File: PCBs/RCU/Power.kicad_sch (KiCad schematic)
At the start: 35 parts, among them J100 Conn_01x02, U100 AP63203WU, U102 AZ1117-3.3, U103 AP63203WU, U104 LM2576S-ADJ

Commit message: Schematic cleanup
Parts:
- C102, C112: value 10u -> (none)
- C106, C107, C110, C111: value 1u -> (none)
- C116: value 100u -> (none)
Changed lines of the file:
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@@
       (effects (font (size 1.27 1.27)) (justify left))
     )
-    (property "Value" "1u" (id 1) (at 92.71 149.86 0)
+    (property "Value" "" (id 1) (at 92.71 149.86 0)
       (effects (font (size 1.27 1.27)) (justify left))
     )
@@
       (effects (font (size 1.27 1.27)) (justify left))
     )
-    (property "Value" "1u" (id 1) (at 90.17 104.14 0)
+    (property "Value" "" (id 1) (at 90.17 104.14 0)
       (effects (font (size 1.27 1.27)) (justify left))
     )
@@
       (effects (font (size 1.27 1.27)) (justify left))
     )
-    (property "Value" "10u" (id 1) (at 198.12 62.23 0)
+    (property "Value" "" (id 1) (at 198.12 62.23 0)
       (effects (font (size 1.27 1.27)) (justify left))
     )
@@
       (effects (font (size 1.27 1.27)) (justify left))
     )
-    (property "Value" "10u" (id 1) (at 196.85 147.32 0)
+    (property "Value" "" (id 1) (at 196.85 147.32 0)
       (effects (font (size 1.27 1.27)) (justify left))
     )
@@
       (effects (font (size 1.27 1.27)) (justify left))
     )
-    (property "Value" "1u" (id 1) (at 119.38 104.14 0)
+    (property "Value" "" (id 1) (at 119.38 104.14 0)
       (effects (font (size 1.27 1.27)) (justify left))
     )
@@
       (effects (font (size 1.27 1.27)) (justify left))
     )
-    (property "Value" "100u" (id 1) (at 189.23 198.12 0)
+    (property "Value" "" (id 1) (at 189.23 198.12 0)
       (effects (font (size 1.27 1.27)) (justify left))
     )
@@
       (effects (font (size 1.27 1.27)) (justify left))
     )
-    (property "Value" "1u" (id 1) (at 121.92 149.86 0)
-      (effects (font (size 1.27 1.27)) (justify left))
-    )
+    (property "Value" "" (id 1) (at 121.92 149.86 0)
+      (effects (font (size 1.27 1.27)) (justify left))
+    )

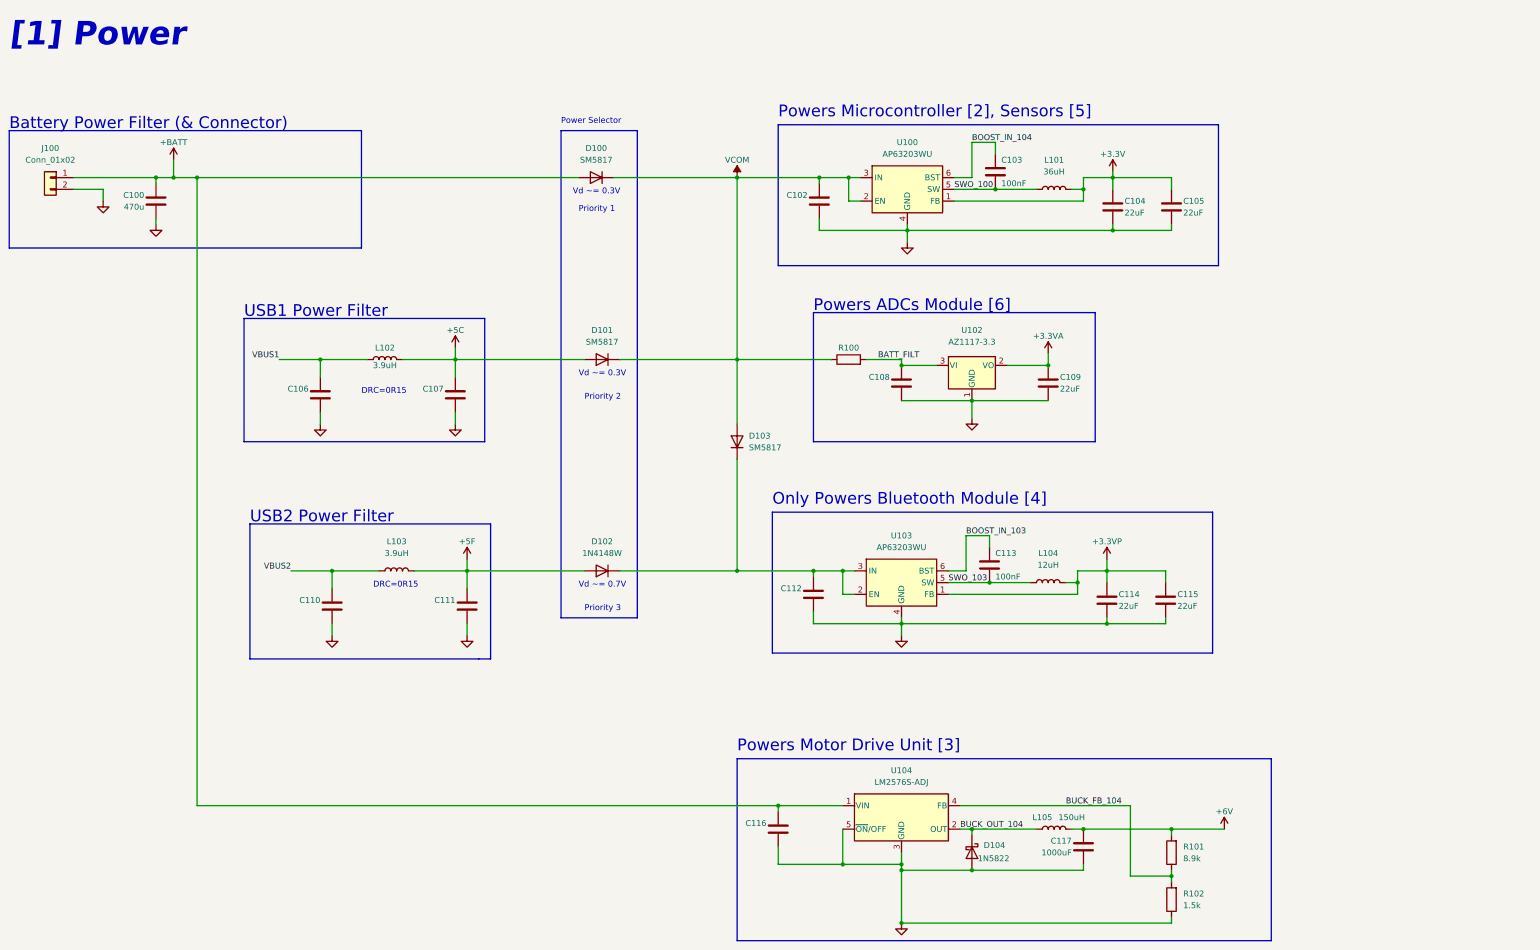
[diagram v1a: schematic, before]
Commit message: Wrote that first regulator in power schematic also powers the external memory
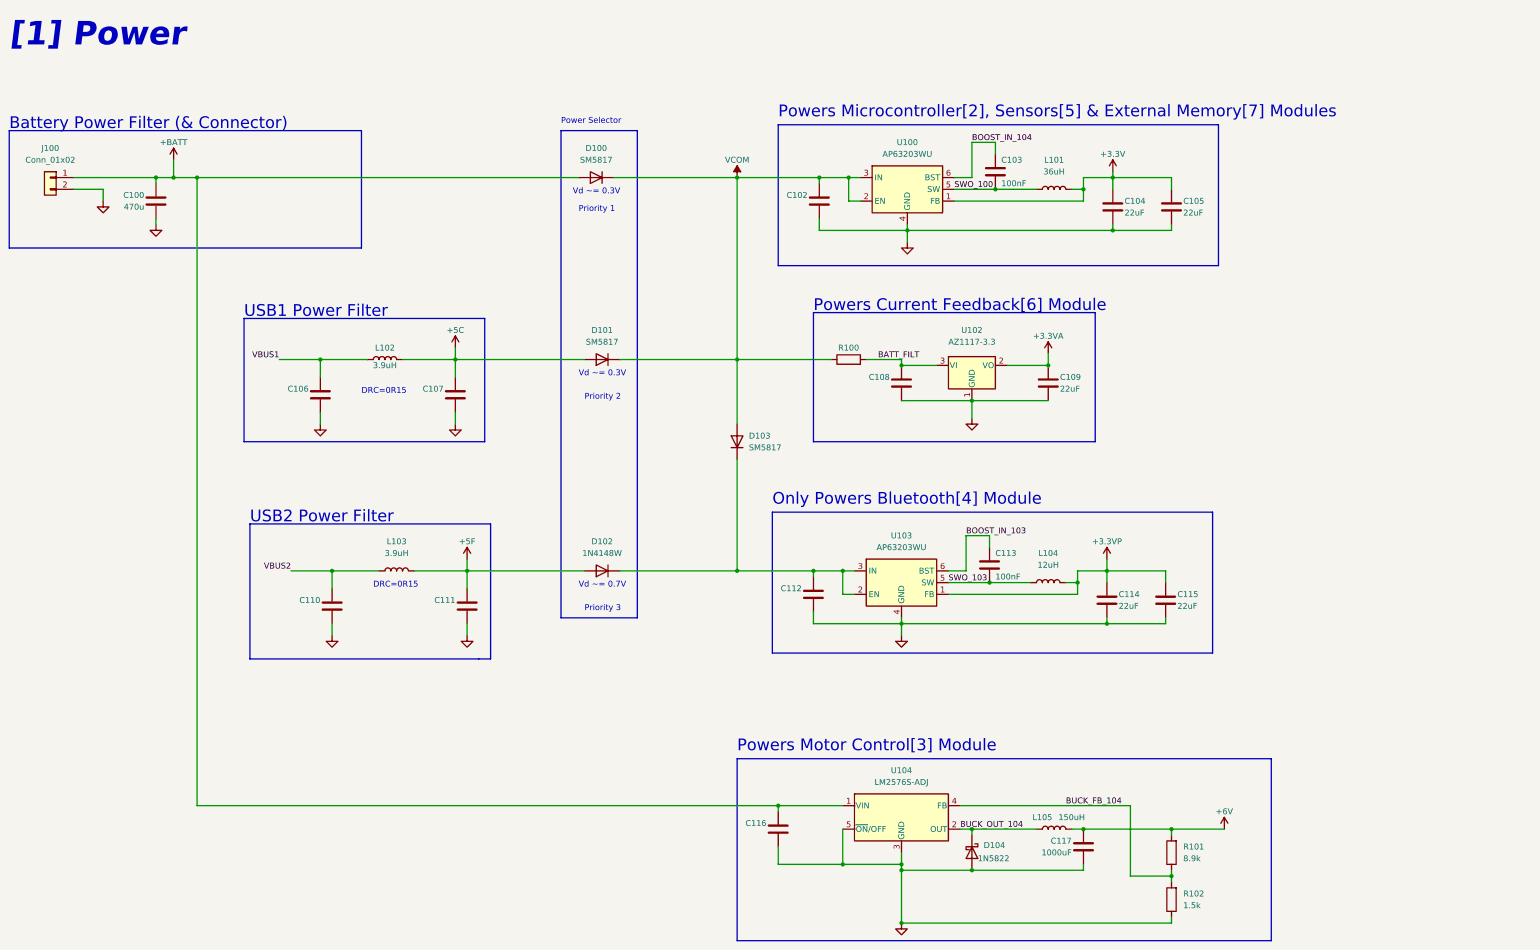
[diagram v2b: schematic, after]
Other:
- note added: "Only Powers Bluetooth[4] Module"
- note added: "Powers Current Feedback[6] Module"
- note added: "Powers Microcontroller[2], Sensors[5] & External Memory[7] Modules"
- note added: "Powers Motor Control[3] Module"
- note removed: "Only Powers Bluetooth Module [4]"
- note removed: "Powers ADCs Module [6]"
- note removed: "Powers Microcontroller [2], Sensors [5]"
- note removed: "Powers Motor Drive Unit [3]"
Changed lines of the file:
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@@
     (effects (font (size 1.27 1.27)) (justify left bottom))
   )
-  (text "Powers Microcontroller [2], Sensors [5]" (at 191.77 43.18 0)
+  (text "Powers Microcontroller[2], Sensors[5] & External Memory[7] Modules"
+    (at 191.77 43.18 0)
     (effects (font (size 2.54 2.54)) (justify left bottom))
   )
@@
     (effects (font (size 1.27 1.27)) (justify left bottom))
   )
-  (text "Powers ADCs Module [6]" (at 199.39 85.09 0)
+  (text "Powers Current Feedback[6] Module " (at 199.39 85.09 0)
     (effects (font (size 2.54 2.54)) (justify left bottom))
   )
-  (text "Only Powers Bluetooth Module [4]" (at 190.5 127 0)
+  (text "Only Powers Bluetooth[4] Module " (at 190.5 127 0)
     (effects (font (size 2.54 2.54)) (justify left bottom))
   )
@@
     (effects (font (size 5.08 5.08) (thickness 1.016) bold italic) (justify left bottom))
   )
-  (text "Powers Motor Drive Unit [3]" (at 182.88 180.34 0)
+  (text "Powers Motor Control[3] Module" (at 182.88 180.34 0)
     (effects (font (size 2.54 2.54)) (justify left bottom))
   )

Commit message: Corrected SPI_MOSI and SPI_MISO labels on U700 - external memory
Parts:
- C102, C112: value (none) -> 10uF
- C106, C107, C110, C111: value (none) -> 1uF
- C108: value (none) -> 22uF
- C116: value (none) -> 100uF
- R100: value (none) -> 5R
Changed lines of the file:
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@@
       (effects (font (size 1.27 1.27)) (justify left))
     )
-    (property "Value" "" (id 1) (at 92.71 149.86 0)
+    (property "Value" "1uF" (id 1) (at 92.71 149.86 0)
       (effects (font (size 1.27 1.27)) (justify left))
     )
@@
       (effects (font (size 1.27 1.27)) (justify left))
     )
-    (property "Value" "" (id 1) (at 215.9 101.6 0)
+    (property "Value" "22uF" (id 1) (at 215.9 101.6 0)
       (effects (font (size 1.27 1.27)) (justify left))
     )
@@
       (effects (font (size 1.27 1.27)) (justify left))
     )
-    (property "Value" "" (id 1) (at 90.17 104.14 0)
+    (property "Value" "1uF" (id 1) (at 90.17 104.14 0)
       (effects (font (size 1.27 1.27)) (justify left))
     )
@@
       (effects (font (size 1.27 1.27)) (justify left))
     )
-    (property "Value" "" (id 1) (at 198.12 62.23 0)
+    (property "Value" "10uF" (id 1) (at 198.12 62.23 0)
       (effects (font (size 1.27 1.27)) (justify left))
     )
@@
       (effects (font (size 1.27 1.27)) (justify left))
     )
-    (property "Value" "" (id 1) (at 196.85 147.32 0)
+    (property "Value" "10uF" (id 1) (at 196.85 147.32 0)
       (effects (font (size 1.27 1.27)) (justify left))
     )
@@
       (effects (font (size 1.27 1.27)) (justify left))
     )
-    (property "Value" "" (id 1) (at 119.38 104.14 0)
+    (property "Value" "1uF" (id 1) (at 119.38 104.14 0)
       (effects (font (size 1.27 1.27)) (justify left))
     )
@@
       (effects (font (size 1.27 1.27)) (justify left))
     )
-    (property "Value" "" (id 1) (at 189.23 198.12 0)
+    (property "Value" "100uF" (id 1) (at 189.23 198.12 0)
       (effects (font (size 1.27 1.27)) (justify left))
     )
@@
     (in_bom yes) (on_board yes)
     (property "Reference" "R100" (id 0) (at 207.01 92.71 90))
-    (property "Value" "" (id 1) (at 207.01 97.79 90))
+    (property "Value" "5R" (id 1) (at 207.01 97.79 90))
     (property "Footprint" "" (id 2) (at 207.01 97.028 90)
       (effects (font (size 1.27 1.27)) hide)
@@
       (effects (font (size 1.27 1.27)) (justify left))
     )
-    (property "Value" "" (id 1) (at 121.92 149.86 0)
-      (effects (font (size 1.27 1.27)) (justify left))
-    )
+    (property "Value" "1uF" (id 1) (at 121.92 149.86 0)
+      (effects (font (size 1.27 1.27)) (justify left))
+    )

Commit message: Have footprints for all power ICs
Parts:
- U102: value AZ1117-3.3 -> (none)
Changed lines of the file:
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@@
     (in_bom yes) (on_board yes) (fields_autoplaced)
     (property "Reference" "U102" (id 0) (at 233.68 88.9 0))
-    (property "Value" "AZ1117-3.3" (id 1) (at 233.68 91.44 0))
+    (property "Value" "" (id 1) (at 233.68 91.44 0))
     (property "Footprint" "" (id 2) (at 233.68 90.17 0)
       (effects (font (size 1.27 1.27) italic) hide)

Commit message: Add footprint to power module diodes, and replaced 1N4148W with 2 SM5817's
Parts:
- removed D102: 1N4148W, Diode_SMD:D_SOD-123, symbol Diode:1N4148W
- added D103, D104: SM5817, Schottky_Diode:SODFL3719X135N, symbol Diode:SM513
- D100, D101: value SM5817 -> (none)
- D102: renamed from D103; value SM5817 -> (none)
- U102: value (none) -> AZ1117-3.3; footprint (none) -> Package_TO_SOT_SMD:TO-252-2
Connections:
- net +5F: now also D103.2 (A)
- net at C112.1, D102.1 (K), U103.2 (EN)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: now also D104.1 (K)
- new net: D103.1 (K), D104.2 (A)
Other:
- note added: "Vd ~= 0.6V"
- note removed: "Vd ~= 0.7V"
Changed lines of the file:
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@@
   (junction (at 276.86 196.85) (diameter 0) (color 0 0 0 0)
   )
+  (junction (at 218.44 204.47) (diameter 0) (color 0 0 0 0)
+  )
+  (junction (at 264.16 55.88) (diameter 0) (color 0 0 0 0)
+  )
+  (junction (at 262.89 152.4) (diameter 0) (color 0 0 0 0)
+  )
+  (junction (at 238.76 58.42) (diameter 0) (color 0 0 0 0)
+  )
+  (junction (at 218.44 96.52) (diameter 0) (color 0 0 0 0)
+  )
+  (junction (at 60.96 55.88) (diameter 0) (color 0 0 0 0)
+  )
+  (junction (at 205.74 204.47) (diameter 0) (color 0 0 0 0)
+  )
+  (junction (at 233.68 104.14) (diameter 0) (color 0 0 0 0)
+  )
   (junction (at 182.88 140.97) (diameter 0) (color 0 0 0 0)
   )
-  (junction (at 218.44 204.47) (diameter 0) (color 0 0 0 0)
-  )
-  (junction (at 264.16 55.88) (diameter 0) (color 0 0 0 0)
-  )
-  (junction (at 262.89 152.4) (diameter 0) (color 0 0 0 0)
-  )
-  (junction (at 238.76 58.42) (diameter 0) (color 0 0 0 0)
-  )
-  (junction (at 218.44 96.52) (diameter 0) (color 0 0 0 0)
-  )
-  (junction (at 60.96 55.88) (diameter 0) (color 0 0 0 0)
-  )
-  (junction (at 205.74 204.47) (diameter 0) (color 0 0 0 0)
-  )
-  (junction (at 233.68 104.14) (diameter 0) (color 0 0 0 0)
-  )
   (junction (at 95.25 140.97) (diameter 0) (color 0 0 0 0)
   )
@@
     (stroke (width 0) (type default) (color 0 0 0 0))
   )
-  (polyline (pts (xy 144.78 45.72) (xy 161.29 45.72))
+  (polyline (pts (xy 143.51 45.72) (xy 162.56 45.72))
     (stroke (width 0) (type default) (color 0 0 0 0))
   )
@@
     (stroke (width 0) (type default) (color 0 0 0 0))
   )
+  (wire (pts (xy 153.67 140.97) (xy 152.4 140.97))
+    (stroke (width 0) (type default) (color 0 0 0 0))
+  )
   (wire (pts (xy 182.88 95.25) (xy 203.2 95.25))
     (stroke (width 0) (type default) (color 0 0 0 0))
@@
     (stroke (width 0) (type default) (color 0 0 0 0))
   )
-  (polyline (pts (xy 144.78 151.13) (xy 161.29 151.13))
+  (polyline (pts (xy 143.51 151.13) (xy 162.56 151.13))
     (stroke (width 0) (type default) (color 0 0 0 0))
   )
@@
     (stroke (width 0) (type default) (color 0 0 0 0))
   )
-  (polyline (pts (xy 144.78 45.72) (xy 144.78 151.13))
+  (polyline (pts (xy 143.51 45.72) (xy 143.51 151.13))
     (stroke (width 0) (type default) (color 0 0 0 0))
   )
@@
     (stroke (width 0) (type default) (color 0 0 0 0))
   )
-  (polyline (pts (xy 161.29 151.13) (xy 161.29 45.72))
+  (polyline (pts (xy 162.56 151.13) (xy 162.56 45.72))
     (stroke (width 0) (type default) (color 0 0 0 0))
   )
@@
     (stroke (width 0) (type default) (color 0 0 0 0))
   )
+  (wire (pts (xy 124.46 140.97) (xy 144.78 140.97))
+    (stroke (width 0) (type default) (color 0 0 0 0))
+  )
+  (wire (pts (xy 161.29 140.97) (xy 182.88 140.97))
+    (stroke (width 0) (type default) (color 0 0 0 0))
+  )
   (wire (pts (xy 110.49 95.25) (xy 121.92 95.25))
     (stroke (width 0) (type default) (color 0 0 0 0))
@@
     (stroke (width 0) (type default) (color 0 0 0 0))
   )
-  (wire (pts (xy 124.46 140.97) (xy 149.86 140.97))
-    (stroke (width 0) (type default) (color 0 0 0 0))
-  )
   (polyline (pts (xy 128.27 113.03) (xy 76.2 113.03))
     (stroke (width 0) (type default) (color 0 0 0 0))
@@
   )
   (polyline (pts (xy 191.77 74.93) (xy 287.02 74.93))
-    (stroke (width 0) (type default) (color 0 0 0 0))
-  )
-  (wire (pts (xy 157.48 140.97) (xy 182.88 140.97))
     (stroke (width 0) (type default) (color 0 0 0 0))
   )
@@
     (effects (font (size 1.27 1.27)) (justify left bottom))
   )
-  (text "Vd ~= 0.7V" (at 148.59 144.78 0)
+  (text "Vd ~= 0.6V" (at 148.59 144.78 0)
     (effects (font (size 1.27 1.27)) (justify left bottom))
   )
@@
     (pin "2")
   )
+  (symbol (lib_id "Diode:SM513") (at 157.48 140.97 180) (unit 1)
+    (in_bom yes) (on_board yes) (fields_autoplaced)
+    (property "Reference" "D104" (id 0) (at 157.48 134.62 0))
+    (property "Value" "SM5817" (id 1) (at 157.48 137.16 0))
+    (property "Footprint" "Schottky_Diode:SODFL3719X135N" (id 2) (at 157.48 136.525 0)
+      (effects (font (size 1.27 1.27)) hide)
+    )
+    (property "Datasheet" "http://cdn-reichelt.de/documents/datenblatt/A400/SMD1N400%23DIO.pdf" (id 3) (at 157.48 140.97 0)
+      (effects (font (size 1.27 1.27)) hide)
+    )
+    (pin "1")
+    (pin "2")
+  )
   (symbol (lib_id "power:GND") (at 57.15 66.04 0) (unit 1)
     (in_bom yes) (on_board yes) (fields_autoplaced)
@@
     )
     (pin "1")
-  )
-  (symbol (lib_id "Diode:1N4148W") (at 153.67 140.97 180) (unit 1)
-    (in_bom yes) (on_board yes) (fields_autoplaced)
-    (property "Reference" "D102" (id 0) (at 153.67 134.62 0))
-    (property "Value" "1N4148W" (id 1) (at 153.67 137.16 0))
-    (property "Footprint" "Diode_SMD:D_SOD-123" (id 2) (at 153.67 136.525 0)
-      (effects (font (size 1.27 1.27)) hide)
-    )
-    (property "Datasheet" "https://www.vishay.com/docs/85748/1n4148w.pdf" (id 3) (at 153.67 140.97 0)
-      (effects (font (size 1.27 1.27)) hide)
-    )
-    (pin "1")
-    (pin "2")
   )
   (symbol (lib_id "power:+3.3VA") (at 250.19 93.98 0) (unit 1)
@@
     (pin "1")
   )
+  (symbol (lib_id "Diode:SM513") (at 148.59 140.97 180) (unit 1)
+    (in_bom yes) (on_board yes) (fields_autoplaced)
+    (property "Reference" "D103" (id 0) (at 148.59 134.62 0))
+    (property "Value" "SM5817" (id 1) (at 148.59 137.16 0))
+    (property "Footprint" "Schottky_Diode:SODFL3719X135N" (id 2) (at 148.59 136.525 0)
+      (effects (font (size 1.27 1.27)) hide)
+    )
+    (property "Datasheet" "http://cdn-reichelt.de/documents/datenblatt/A400/SMD1N400%23DIO.pdf" (id 3) (at 148.59 140.97 0)
+      (effects (font (size 1.27 1.27)) hide)
+    )
+    (pin "1")
+    (pin "2")
+  )
   (symbol (lib_id "power:GND") (at 218.44 217.17 0) (unit 1)
     (in_bom yes) (on_board yes) (fields_autoplaced)
@@
     (in_bom yes) (on_board yes) (fields_autoplaced)
     (property "Reference" "U102" (id 0) (at 233.68 88.9 0))
-    (property "Value" "" (id 1) (at 233.68 91.44 0))
-    (property "Footprint" "" (id 2) (at 233.68 90.17 0)
+    (property "Value" "AZ1117-3.3" (id 1) (at 233.68 91.44 0))
+    (property "Footprint" "Package_TO_SOT_SMD:TO-252-2" (id 2) (at 233.68 90.17 0)
       (effects (font (size 1.27 1.27) italic) hide)
     )
@@
     (in_bom yes) (on_board yes) (fields_autoplaced)
     (property "Reference" "D100" (id 0) (at 152.4 49.53 0))
-    (property "Value" "SM5817" (id 1) (at 152.4 52.07 0))
+    (property "Value" "" (id 1) (at 152.4 52.07 0))
     (property "Footprint" "" (id 2) (at 152.4 51.435 0)
       (effects (font (size 1.27 1.27)) hide)
@@
   (symbol (lib_id "Diode:SM513") (at 182.88 113.03 90) (unit 1)
     (in_bom yes) (on_board yes) (fields_autoplaced)
-    (property "Reference" "D103" (id 0) (at 185.42 111.7599 90)
+    (property "Reference" "D102" (id 0) (at 185.42 111.7599 90)
       (effects (font (size 1.27 1.27)) (justify right))
     )
-    (property "Value" "SM5817" (id 1) (at 185.42 114.2999 90)
+    (property "Value" "" (id 1) (at 185.42 114.2999 90)
       (effects (font (size 1.27 1.27)) (justify right))
     )
@@
     (in_bom yes) (on_board yes) (fields_autoplaced)
     (property "Reference" "D101" (id 0) (at 153.67 88.9 0))
-    (property "Value" "SM5817" (id 1) (at 153.67 91.44 0))
+    (property "Value" "" (id 1) (at 153.67 91.44 0))
     (property "Footprint" "" (id 2) (at 153.67 90.805 0)
       (effects (font (size 1.27 1.27)) hide)

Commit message: Add soler wire connections for battery power
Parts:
- J100: value Conn_01x02 -> (none)
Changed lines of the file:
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@@
     (in_bom yes) (on_board yes) (fields_autoplaced)
     (property "Reference" "J100" (id 0) (at 34.29 49.53 0))
-    (property "Value" "Conn_01x02" (id 1) (at 34.29 52.07 0))
+    (property "Value" "" (id 1) (at 34.29 52.07 0))
     (property "Footprint" "" (id 2) (at 34.29 55.88 0)
       (effects (font (size 1.27 1.27)) hide)

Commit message: Add fooprint for TVS diode, tactile switch and crystal in [2]
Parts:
- D100, D101, D102: value (none) -> SM5817; footprint (none) -> Schottky_Diode:SODFL3719X135N
- J100: value (none) -> Conn_01x02; footprint (none) -> Connector_Wire:SolderWire-2sqmm_1x02_P7.8mm_D2mm_OD3.9mm
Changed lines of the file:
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@@
     (in_bom yes) (on_board yes) (fields_autoplaced)
     (property "Reference" "J100" (id 0) (at 34.29 49.53 0))
-    (property "Value" "" (id 1) (at 34.29 52.07 0))
-    (property "Footprint" "" (id 2) (at 34.29 55.88 0)
+    (property "Value" "Conn_01x02" (id 1) (at 34.29 52.07 0))
+    (property "Footprint" "Connector_Wire:SolderWire-2sqmm_1x02_P7.8mm_D2mm_OD3.9mm" (id 2) (at 34.29 55.88 0)
       (effects (font (size 1.27 1.27)) hide)
     )
@@
     (in_bom yes) (on_board yes) (fields_autoplaced)
     (property "Reference" "D100" (id 0) (at 152.4 49.53 0))
-    (property "Value" "" (id 1) (at 152.4 52.07 0))
-    (property "Footprint" "" (id 2) (at 152.4 51.435 0)
+    (property "Value" "SM5817" (id 1) (at 152.4 52.07 0))
+    (property "Footprint" "Schottky_Diode:SODFL3719X135N" (id 2) (at 152.4 51.435 0)
       (effects (font (size 1.27 1.27)) hide)
     )
@@
       (effects (font (size 1.27 1.27)) (justify right))
     )
-    (property "Value" "" (id 1) (at 185.42 114.2999 90)
+    (property "Value" "SM5817" (id 1) (at 185.42 114.2999 90)
       (effects (font (size 1.27 1.27)) (justify right))
     )
-    (property "Footprint" "" (id 2) (at 187.325 113.03 0)
+    (property "Footprint" "Schottky_Diode:SODFL3719X135N" (id 2) (at 187.325 113.03 0)
       (effects (font (size 1.27 1.27)) hide)
     )
@@
     (in_bom yes) (on_board yes) (fields_autoplaced)
     (property "Reference" "D101" (id 0) (at 153.67 88.9 0))
-    (property "Value" "" (id 1) (at 153.67 91.44 0))
-    (property "Footprint" "" (id 2) (at 153.67 90.805 0)
-      (effects (font (size 1.27 1.27)) hide)
-    )
+    (property "Value" "SM5817" (id 1) (at 153.67 91.44 0))
+    (property "Footprint" "Schottky_Diode:SODFL3719X135N" (id 2) (at 153.67 90.805 0)
+      (effects (font (size 1.27 1.27)) hide)
+    )
